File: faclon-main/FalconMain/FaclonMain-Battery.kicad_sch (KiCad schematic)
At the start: 0 parts

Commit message: Reorganize
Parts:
- added C13, C16: 220nF, Capacitor_SMD:C_0603_1608Metric, symbol Device:C_Small
- added C14: 100uF, Capacitor_THT:CP_Radial_D8.0mm_P3.50mm, symbol Device:C_Polarized_Small
- added C15, C20, C22, C23, C28: 1uF, Capacitor_SMD:C_0603_1608Metric, symbol Device:C_Small
- added C17, C19: 10nF, Capacitor_SMD:C_0402_1005Metric, symbol Device:C_Small
- added C18: 10uF, Capacitor_SMD:C_1210_3225Metric, symbol Device:C_Small
- added C21, C24: 47nF, Capacitor_SMD:C_0402_1005Metric, symbol Device:C_Small
- added C25: 33uF, Capacitor_THT:CP_Radial_D6.3mm_P2.50mm, symbol Device:C_Polarized_Small
- added C26: 100nF, Capacitor_SMD:C_0402_1005Metric, symbol Device:C_Small
- added C27: 1nF, Capacitor_SMD:C_0402_1005Metric, symbol Device:C_Small
- added D1: 20A, JetkovKiCADLib:TO-252-2-3_DPAK_ST, symbol JetkovKiCADLib:D_Schottky_AAK_Small
- added L2: 22uH, JetkovKiCADLib:DR125-220-R_Handsolder, symbol Device:L_Small
- added Q1, Q11, Q12, Q2, Q4, Q6, Q8, Q9: Q_PMOS_GSD, JetkovKiCADLib:SC-96_TSMT3_ROM, symbol Device:Q_PMOS_GSD
- added Q10, Q13, Q14, Q3, Q7: Q_NMOS_GSD, JetkovKiCADLib:SOT-323_SC-70, symbol Device:Q_NMOS_GSD
- added Q15, Q16, Q5: Q_PMOS_LFPAK, JetkovKiCADLib:LFPACK56-S08_SOT669_NXP, symbol JetkovKiCADLib:Q_PMOS_LFPAK
- added R10, R11: 4.7R, Resistor_SMD:R_0402_1005Metric, symbol Device:R_Small
- added R12, R17, R26, R32, R34: 49.9k, Resistor_SMD:R_0402_1005Metric, symbol Device:R_Small
- added R13, R19, R28, R36: 47R, Resistor_SMD:R_2512_6332Metric, symbol Device:R_Small
- added R14, R15, R21, R23, R27, R30, R33, R37, R38, R6, R8: 100k, Resistor_SMD:R_0402_1005Metric, symbol Device:R_Small
- added R16: 154k, Resistor_SMD:R_0402_1005Metric, symbol Device:R_Small
- added R18, R20, R40: 0R, Resistor_SMD:R_0402_1005Metric, symbol Device:R_Small
- added R22: 68m, Resistor_SMD:R_0612_1632Metric, symbol Device:R_Small
- added R24: 86.6k, Resistor_SMD:R_0402_1005Metric, symbol Device:R_Small
- added R25: DNP, Resistor_SMD:R_0402_1005Metric, symbol Device:R_Small
- added R29, R35: 133k, Resistor_SMD:R_0402_1005Metric, symbol Device:R_Small
- added R31: 10k, Resistor_SMD:R_0402_1005Metric, symbol Device:R_Small
- added R39: 442k, Resistor_SMD:R_0402_1005Metric, symbol Device:R_Small
- added R7: 221k, Resistor_SMD:R_0402_1005Metric, symbol Device:R_Small
- added R9: 22m, Resistor_SMD:R_1206_3216Metric, symbol Device:R_Small
- added U2: MAX1873TEEE+, JetkovKiCADLib:16-SSOP_16-QSOP_MAX, symbol JetkovKiCADLib:MAX1873TEEE+
- added U3: LTC4412ES6#TRPBF, JetkovKiCADLib:SOT-23-6_TSOT-23-6_LT, symbol JetkovKiCADLib:LTC4412ES6#TRPBF
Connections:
- new net: Q6.3 (D), R19.1
- new net: Q1.1 (G), Q11.1 (G), Q14.3 (D), Q4.1 (G), Q8.1 (G), R8.1
- new net: Q1.3 (D), R7.2
- new net: Q4.3 (D), R16.2
- new net: C18.2, U2.16 (VL)
- new net: C23.1, R25.1, R29.1, U2.9 (REF)
- new net: R29.2, R32.1, U2.8 (VADJ)
- new net: Q12.3 (D), R36.1
- new net: Q5.4 (G), U2.14 (EXT)
- new net: D1.3 (K), L2.1, Q5.5 (D)
- new net: Q11.3 (D), R34.2
- new net: C17.1, R10.2, U2.2 (CSSP)
- new net: C19.1, R11.2, U2.1 (CSSN)
- new net: L2.2, R22.2, U2.11 (CSB)
- new net: C16.1, U2.13 (VH)
- new net: C24.2, U2.3 (CCS)
- new net: C27.2, R31.2, U2.4 (CCV)
- new net: C21.2, U2.5 (CCI)
- new net: R20.1, R25.2, R27.1, U2.6 (ICHG/EN)
- new net: R18.1, U2.7 (IOUT)
- new net: Q9.3 (D), R28.1
- new net: R40.2, U3.3 (CTL)
- new net: Q16.4 (G), U3.5 (GATE)
- new net: Q2.3 (D), R13.1
- new net: C26.2, R31.1
- new net: Q8.3 (D), R24.2
- new net: Q15.4 (G), R39.1, U3.4 (STAT)
- new net +19V5: Q15.5 (D)
- new net CELL_1S: Q11.2 (S), Q12.2 (S), R28.2, R33.2
- new net CELL_2S: Q8.2 (S), Q9.2 (S), R19.2, R23.2
- new net CELL_3S: Q4.2 (S), Q6.2 (S), R13.2, R15.2
- new net CELL_4S: Q1.2 (S), Q2.2 (S), R6.2, R8.2
- new net CHG_IOUT: R18.2
- new net EN_CELL_1S_DIS: Q13.1 (G), R37.2
- new net EN_CELL_2S_DIS: Q10.1 (G), R30.2
- new net EN_CELL_3S_DIS: Q7.1 (G), R21.2
- new net EN_CELL_4S_DIS: Q3.1 (G), R14.2
- new net EN_CELL_SENSE: Q14.1 (G), R38.2
- new net GND: C13.2, C14.2, C15.2, C17.2, C18.1, C19.2, C20.2, C21.1, C22.2, C23.2, C24.1, C25.2, C26.1, C27.1, C28.2, D1.1 (A), D1.2 (A), Q10.2 (S), Q13.2 (S), Q14.2 (S), Q3.2 (S), Q7.2 (S), R12.1, R14.1, R17.1, R21.1, R26.1, R27.2, R30.1, R32.2, R35.1, R36.2, R37.1, R38.1, R40.1, U2.12 (GND), U3.2 (GND)
- new net VBAT: C25.1, Q16.5 (D), R22.1, U2.10 (BATT), U3.1 (VIN)
- new net VDC: C13.1, C16.2, Q15.1 (S), Q15.2 (S), Q15.3 (S), Q16.1 (S), Q16.2 (S), Q16.3 (S), R10.1, R39.2, R9.1, U2.15 (DCIN), U3.6 (SENSE)
- new net VSENSE_CELL_1S: C28.1, R34.1, R35.2
- new net VSENSE_CELL_2S: C22.1, R24.1, R26.2
- new net VSENSE_CELL_3S: C20.1, R16.1, R17.2
- new net VSENSE_CELL_4S: C15.1, R12.2, R7.1
- new net VSET_ICHG: R20.2
- new net VSYS: C14.1, Q5.1 (S), Q5.2 (S), Q5.3 (S), R11.1, R9.2
- new net ~{EN_CELL_1S_DIS}: Q12.1 (G), Q13.3 (D), R33.1
- new net ~{EN_CELL_2S_DIS}: Q10.3 (D), Q9.1 (G), R23.1
- new net ~{EN_CELL_3S_DIS}: Q6.1 (G), Q7.3 (D), R15.1
- new net ~{EN_CELL_4S_DIS}: Q2.1 (G), Q3.3 (D), R6.1
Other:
- note added: "4.2V"
- note added: "AC/DC Adapter Current Limiting -------------------- I_{IN(MAX)}=0.1V/R_{CSS} =0.1V/22mOhms =4.55A"
- note added: "AC/DC and Battery Power OR-ing"
- note added: "BATTERY BALANCING"
- note added: "BATTERY CHARGING"
- note added: "Cell Voltage Cutoff Set -------------------- V_{VADJ}=9.5(V_{CELL})-9(V_{REF}) =9.5(4.1V)-9(4.2V)=1.15V R_{2}=R_{1}[V_{VADJ}/(V_{REF}-V_{VADJ})] =133k*(1.15/(4.2-1.15)~=49.9k V_{VADJ}=1.14587V V_{CELL}=(1.14587V+9(4.2V))/9.5=4.0996V"
- note added: "Charge Current Sense Output -------------------- V_{Iout}=20(R_{CSB} * I_{chg}) =20(0.068)(2.3)=3.2V C_{load} < 5nF Charge Current Set -------------------- V_{ICH-EN}=I_{CHG} * 1.3146"
- note added: "Charger enabled if DCIN>BATT+220mV Charger disabled if DCIN<BATT+50mV"
- note added: "EXT drives to DCIN-5V"
- note added: "FETs prevent current injection into MCU IO pins when MCU is unpowered"
- note added: "H: VSYS L: VSYS-4.42V"
- note added: "Heatsink"
- note added: "I_{off}=10uA P_{off}=148uW"
- note added: "Keep divider above (n/4)*200k to reduce effect of R_{ds} and reduce power draw"
- note added: "Li-ion 4S Charge Regulator Controller"
- note added: "Li-ion Cell Balancing FETs"
- note added: "Li-ion Cell Voltage Sensing"
- note added: "Max Charge Current Set -------------------- R_{CSB}=0.2V(V_{ICH-EN}/V_{REF})/I_{CHG} =0.2V(3.3V/4.2V)/2.5A ~=62.6mOhms I_{CHG}=0.2V(3.3V/4.2V)/0.068Ohms=2.311A"
- note added: "Minimum Inductance -------------------- L>{V_{BATT}[V_{DCIN(MAX)}-V_{BATT}]}/{[V_{DCIN(MAX)}][f_{SW}][I_{CHG}][LIR]} >((14.8V)(19.5V-14.8V))/((19.5V)(300kHz)(2.5A)(0.3)) >15.85uH"
- note added: "Minimum Output Capacitance -------------------- C_{OUT}>4.2(1+16.8/18.5)/[(16.8)(300e3)(62.6e-3)]=25.4uF R_{ESR}<0.0626*12/4.2=179mOhms"
- note added: "Note: Measured voltage may be 50mV lower than true if measured while a discharge FET is conducting (due to parasitic fuse, etc. resistance)"
- note added: "Place dividers and caps close to MCU pins"
- note added: "R_{TH}=(R_{1}//R_{2}) R_{TH(MAX)}=42.7k"
- note added: "STAT low when SENSE>VIN+20mV Vf of FET Diode < 19.5-17-0.02=2.48V"
- note added: "T_{RC}=(R1//R2)*C C<(1/42.7k)=23.4uF"
- note added: "VDC=VBAT if charger is discconected"
- note added: "Vf(diode)=0.8V"
- note added: "[ST: AN2834] C>131nF"

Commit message: Layout WIP
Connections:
- net CHG_DRN: now reaches D1.3 (K), L2.1, Q5.5 (D)
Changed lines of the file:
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@@
   (junction (at 148.59 163.83) (diameter 0) (color 0 0 0 0)
   )
+  (junction (at 113.03 72.39) (diameter 0) (color 0 0 0 0)
+  )
   (junction (at 113.03 95.25) (diameter 0) (color 0 0 0 0)
   )
@@
   )
   (wire (pts (xy 182.88 59.69) (xy 182.88 62.23))
+    (stroke (width 0) (type default) (color 0 0 0 0))
+  )
+  (wire (pts (xy 113.03 72.39) (xy 123.19 72.39))
     (stroke (width 0) (type default) (color 0 0 0 0))
   )
@@
     (effects (font (size 2 2)) (justify left bottom))
   )
-  (text "Heatsink" (at 110.49 71.12 0)
+  (text "Heatsink" (at 110.49 64.77 0)
     (effects (font (size 1.27 1.27) (thickness 0.254) bold) (justify left bottom))
   )
@@
     (effects (font (size 1.27 1.27)) (justify right bottom))
   )
+  (label "CHG_DRN" (at 123.19 72.39 180)
+    (effects (font (size 1.27 1.27)) (justify right bottom))
+  )

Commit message: Layout WIP
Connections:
- net CHG_DRV: now reaches Q5.4 (G), U2.14 (EXT)
- net CHG_CSSP: now reaches C17.1, R10.2, U2.2 (CSSP)
- net CHG_CSSN: now reaches C19.1, R11.2, U2.1 (CSSN)
- net CHG_CSB: now reaches L2.2, R22.2, U2.11 (CSB)
- net PWR_OR_GATE: now reaches Q16.4 (G), U3.5 (GATE)
- net PWR_OR_STAT: now reaches Q15.4 (G), R39.1, U3.4 (STAT)
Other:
- moved on the sheet: Q15, Q16, R39, R40, U3

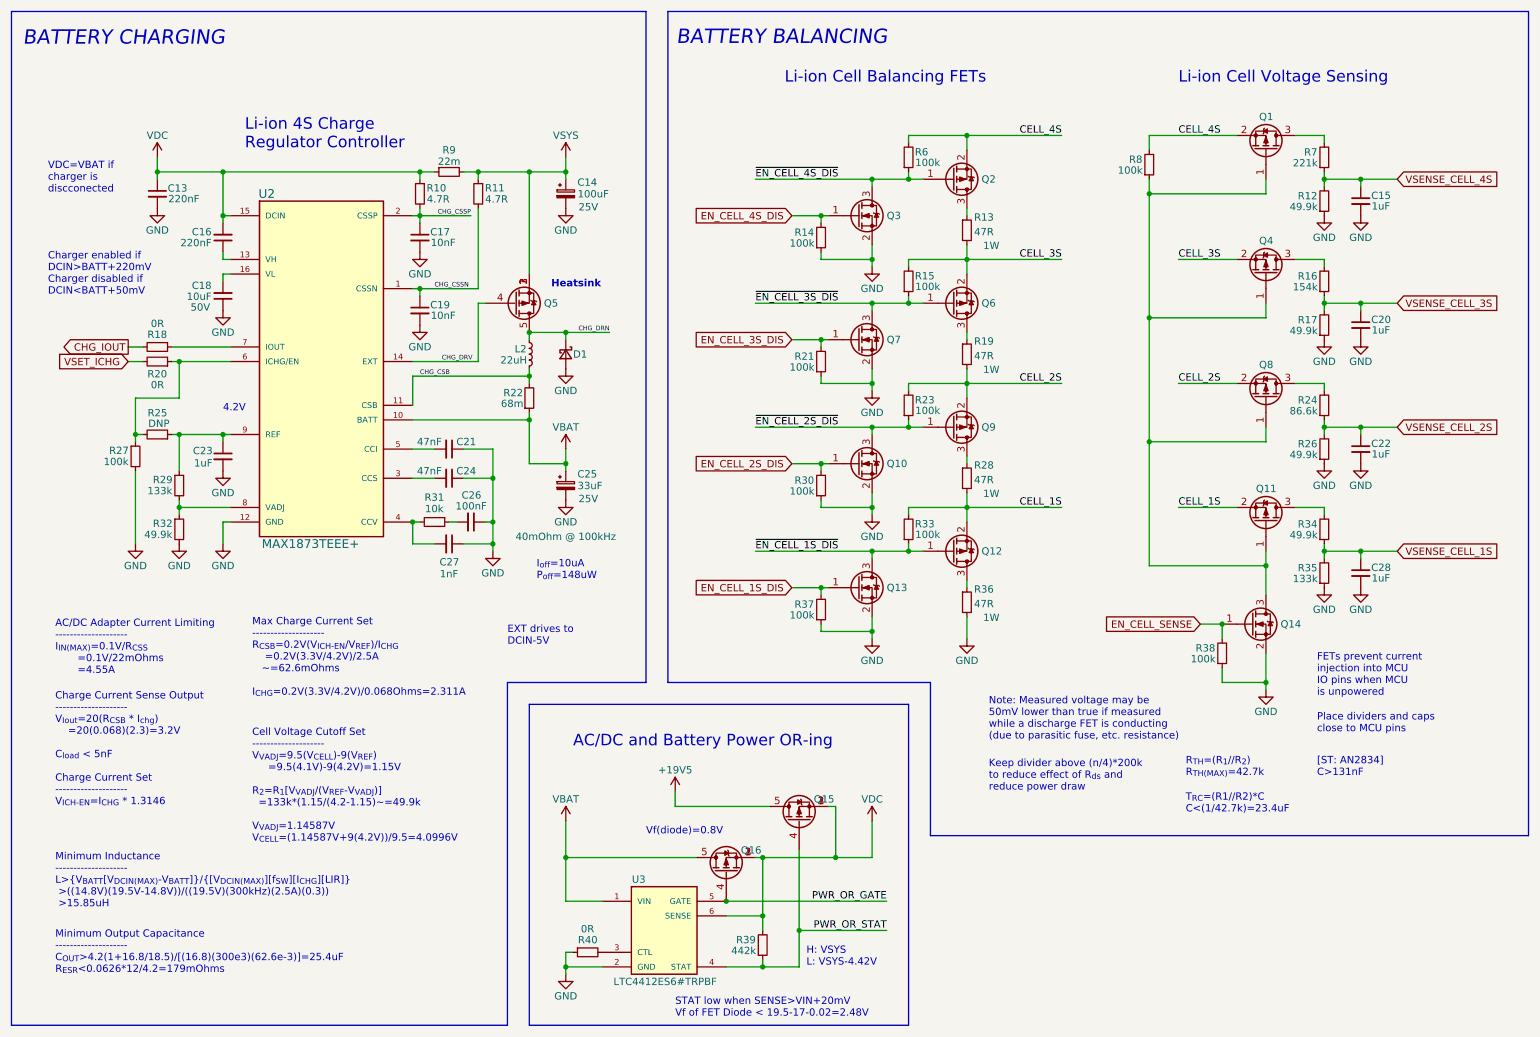
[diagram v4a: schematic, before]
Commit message: Large component rough placement
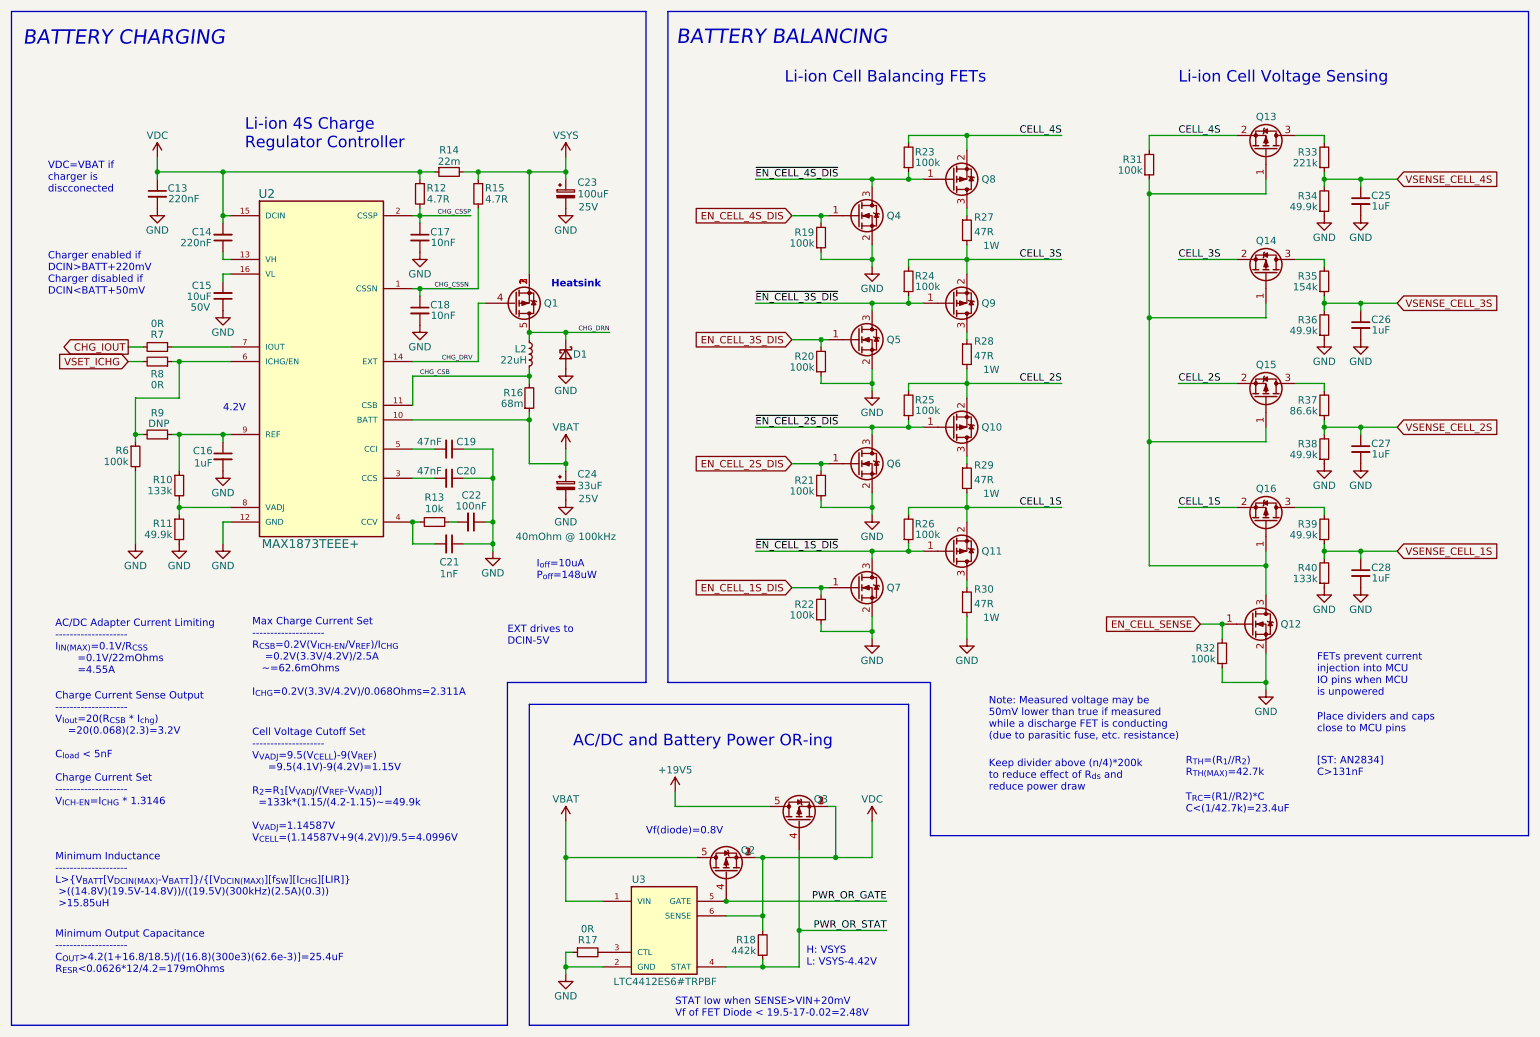
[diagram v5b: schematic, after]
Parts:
- C24: renamed from C25; footprint Capacitor_THT:CP_Radial_D6.3mm_P2.50mm -> JetkovKiCADLib:CP_Radial_D6.3mm_P2.50mm
- renumbered C16 to C14, C18 to C15, C23 to C16, C19 to C18, C21 to C19, C24 to C20, C27 to C21, C26 to C22, C14 to C23, C15 to C25, C20 to C26, C22 to C27, Q5 to Q1, Q9 to Q10, Q12 to Q11, Q14 to Q12, Q1 to Q13, Q4 to Q14, Q8 to Q15, Q11 to Q16, Q16 to Q2, Q15 to Q3, Q3 to Q4, Q7 to Q5, Q10 to Q6, Q13 to Q7, Q2 to Q8, Q6 to Q9, R29 to R10, R32 to R11, R10 to R12, R31 to R13, R9 to R14, R11 to R15, R22 to R16, R40 to R17, R39 to R18, R14 to R19, R21 to R20, R30 to R21, R37 to R22, R6 to R23, R15 to R24, R23 to R25, R33 to R26, R13 to R27, R19 to R28, R28 to R29, R36 to R30, R8 to R31, R38 to R32, R7 to R33, R12 to R34, R16 to R35, R17 to R36, R24 to R37, R26 to R38, R34 to R39, R35 to R40, R27 to R6, R18 to R7, R20 to R8, R25 to R9

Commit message: Rought placement done
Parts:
- added C13, C17: 1uF, Capacitor_SMD:C_0603_1608Metric, symbol Device:C_Small
- C15: value 10uF -> 1uF; footprint Capacitor_SMD:C_1210_3225Metric -> Capacitor_SMD:C_0603_1608Metric; Part Number CGA6P3X7S1H106K250AB -> CGA3E1X7R1E105K080AC; Voltage 50V -> 25V
- renumbered C13 to C14, C14 to C16, C16 to C18, C17 to C19, C18 to C20, C19 to C21, C20 to C22, C21 to C23, C22 to C24, C23 to C25, C24 to C26, C25 to C27, C26 to C28, C27 to C29, C28 to C30
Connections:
- net GND: now also C15.2, C13.2, C17.2; no longer C15.1
- net at U2.16 (VL): now also C15.1, C13.1, C17.1; no longer C15.2

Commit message: Reviewed again
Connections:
- net CHG_VREF: now reaches C18.1, R10.1, R9.1, U2.9 (REF)
- net CHG_VADJ: now reaches R10.2, R11.1, U2.8 (VADJ)
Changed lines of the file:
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@@
     (effects (font (size 1.27 1.27)) (justify left bottom))
+  )
+  (label "CHG_VREF" (at 46.99 90.17 0)
+    (effects (font (size 0.8 0.8)) (justify left bottom))
   )
   (label "CHG_CSSP" (at 96.52 52.07 180)
@@
     (effects (font (size 1.27 1.27)) (justify left bottom))
   )
+  (label "CHG_VADJ" (at 46.99 102.87 0)
+    (effects (font (size 0.8 0.8)) (justify left bottom))
+  )
   (global_label "VSENSE_CELL_3S" (shape input) (at 257.81 67.31 0) (fields_autoplaced)

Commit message: Layour WIP
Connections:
- net CHG_IEN: now reaches R6.1, R8.1, R9.2, U2.6 (ICHG/EN)
- net CHG_IOUT0: now reaches R7.1, U2.7 (IOUT)
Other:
- moved on the sheet: R31
